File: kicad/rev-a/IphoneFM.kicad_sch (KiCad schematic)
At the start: 102 parts, among them J1 USB 2.0 Type-C, J2 SMA jack, SW1 SPDT, SW2 SPST, SW3 6 × SPST, U1 MCU, U2 Synthesizer, U3 3.3 V 600 mA LDO, U4 FM receiver, U5 SPDT RF switch, U6 USB ESD array, U7 Digital step attenuator, Y2 20 MHz CMOS XO

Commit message: Step 2.6: IphoneFM footprints assigned to all 102 symbols
Co-Authored-By: Claude Opus 5.5 <noreply@anthropic.com>
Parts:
- C1, C2, C23, C27, C8: footprint Capacitor_SMD:C_0603_1608Metric -> IphoneFM:C_0603_1608Metric
- C10, C11, C13, C14, C15, C16, C17, C18, C19, C20, C21, C22, C24, C25, C26, C28, C29, C30, C31, C32, C33, C34, C35, C36, C37, C38, C39, C4, C40, C41, C5, C6, C7: footprint Capacitor_SMD:C_0402_1005Metric -> IphoneFM:C_0402_1005Metric
- C12, C3, C9: footprint Capacitor_SMD:C_0805_2012Metric -> IphoneFM:C_0805_2012Metric
- D1: footprint (none) -> IphoneFM:LED_RGB_XINGLIGHT_XL-1615RGBC_1.6x1.5mm
- D3, D4: footprint Package_SON:Texas_DPY0002A_0.6x1mm_P0.65mm -> IphoneFM:Texas_DPY0002A_0.6x1mm_P0.65mm
- D5: footprint (none) -> IphoneFM:D_SOD-882
- FB1, FB2, FB3: footprint Inductor_SMD:L_0402_1005Metric -> IphoneFM:L_0402_1005Metric
- J1: footprint (none) -> IphoneFM:USB_C_Receptacle_HRO_TYPE-C-31-M-12_2020
- J2: footprint (none) -> IphoneFM:SMA_BAT_Wireless_BWSMA-KWE-Z001
- L1, L2, L3: footprint Inductor_SMD:L_0603_1608Metric -> IphoneFM:L_0603_1608Metric
- R1, R10, R11, R12, R13, R14, R15, R16, R17, R18, R19, R2, R20, R21, R22, R23, R24, R25, R26, R27, R3, R4, R5, R6, R7, R8, R9: footprint Resistor_SMD:R_0402_1005Metric -> IphoneFM:R_0402_1005Metric
- RV1, RV2, RV3: footprint (none) -> IphoneFM:Potentiometer_Alps_RK10J_Reflow_Thumbwheel_14mm
- SW1: footprint (none) -> IphoneFM:SW_SPDT_Shouhan_MSK12C02_Tabs4
- SW2: footprint (none) -> IphoneFM:SW_SPST_EVQP7A
- SW3: footprint (none) -> IphoneFM:SW_DIP_SPSTx06_Side_CK_TDP06H1SBD1_W7.62mm_P1.27mm
- TP1, TP2, TP3, TP4, TP5, TP6, TP7, TP8: footprint TestPoint:TestPoint_Pad_D1.5mm -> IphoneFM:TestPoint_Pad_D1.5mm
- U1: footprint Package_DFN_QFN:QFN-48-1EP_7x7mm_P0.5mm_EP5.6x5.6mm -> IphoneFM:QFN-48-1EP_7x7mm_P0.5mm_EP5.6x5.6mm
- U2: footprint (none) -> IphoneFM:TI_NJK0036A_WQFN-36-1EP_6x6mm_P0.5mm_EP4.6x4.6mm
- U3: footprint Package_TO_SOT_SMD:SOT-23-5 -> IphoneFM:SOT-23-5
- U4: footprint (none) -> IphoneFM:SiliconLabs_QFN-20-1EP_3x3mm_P0.5mm_EP1.8x1.8mm
- U5: footprint (none) -> IphoneFM:SOT-363_SC-70-6
- U6: footprint Package_TO_SOT_SMD:SOT-23-6 -> IphoneFM:SOT-23-6
- U7: footprint (none) -> IphoneFM:QFN-24-1EP_4x4mm_P0.5mm_EP2.75x2.75mm
- Y2: footprint (none) -> IphoneFM:Oscillator_SMD_SiT_PQFN-4Pin_3.2x2.5mm

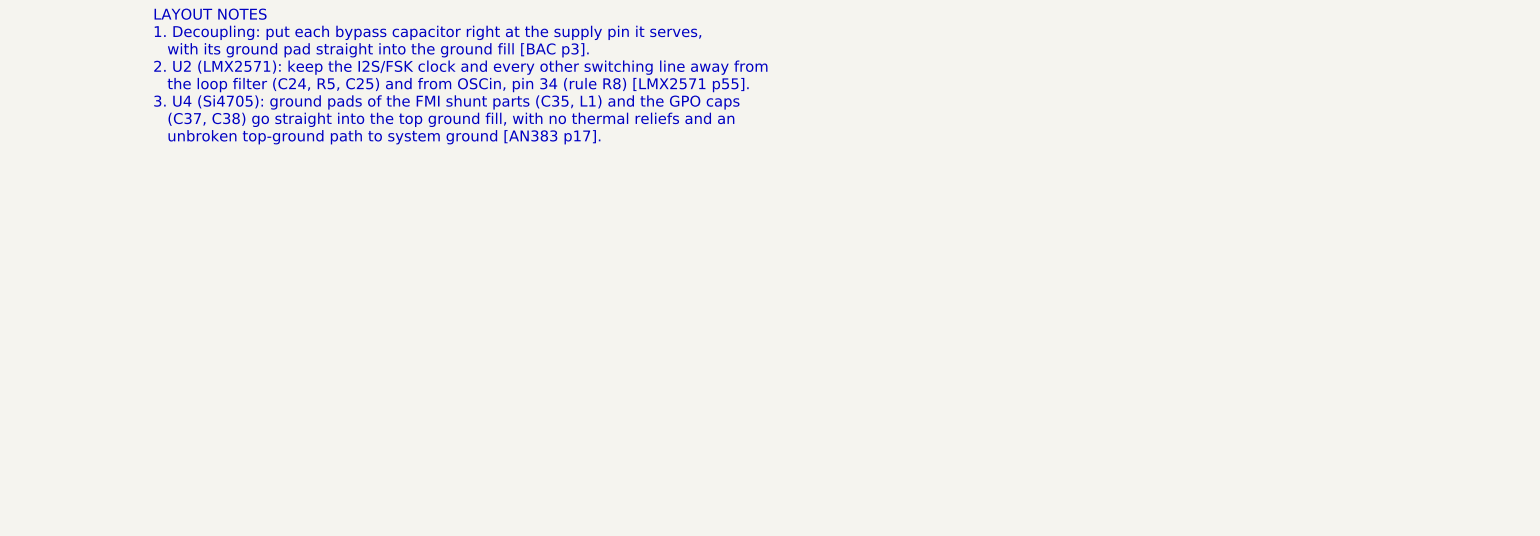
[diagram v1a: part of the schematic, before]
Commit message: Step 3.5: mounting holes H1-H4 in netlist.json, on the schematic, with an M2 footprint
Co-Authored-By: Claude Opus 5.5 <noreply@anthropic.com>
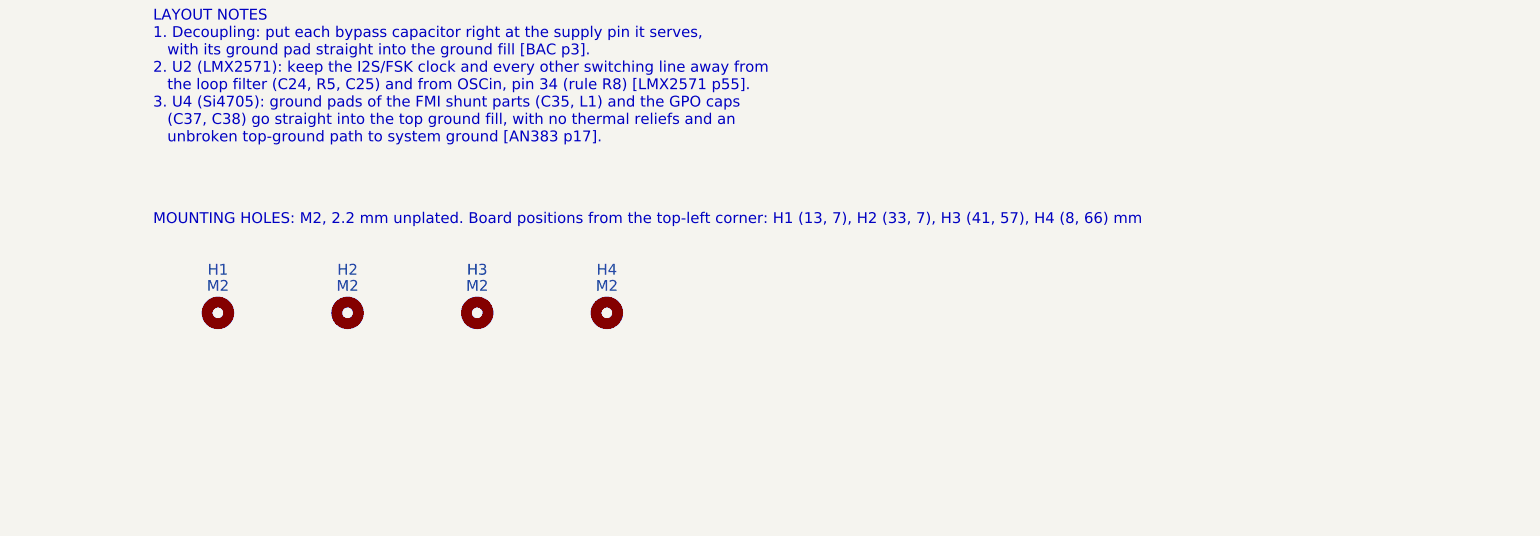
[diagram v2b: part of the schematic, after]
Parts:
- added H1, H2, H3, H4: M2, IphoneFM:MountingHole_2.2mm_M2, symbol Mechanical:MountingHole
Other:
- note added: "MOUNTING HOLES: M2, 2.2 mm unplated. Board positions from the top-left corner: H1 (13, 7), H2 (33, 7), H3 (41, 57), H4 (8, 66) mm"
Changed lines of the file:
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@@
 		(effects (font (size 1.27 1.27)) (justify left top))
+	)
+	(symbol
+		(lib_id "Mechanical:MountingHole")
+		(at 452.12 358.14 0)
+		(unit 1)
+		(exclude_from_sim no)
+		(in_bom no)
+		(on_board yes)
+		(dnp no)
+		(property "Reference" "H1"
+			(at 452.12 353.06 0)
+			(effects (font (size 1.27 1.27)))
+		)
+		(property "Value" "M2"
+			(at 452.12 354.96 0)
+			(effects (font (size 1.27 1.27)))
+		)
+		(property "Footprint" "IphoneFM:MountingHole_2.2mm_M2"
+			(at 452.12 358.14 0)
+			(effects (font (size 1.27 1.27)) (hide yes))
+		)
+		(property "Datasheet" "~"
+			(at 452.12 358.14 0)
+			(effects (font (size 1.27 1.27)) (hide yes))
+		)
+		(instances
+			(project "IphoneFM"
+				(path "/efee88c9-028d-4fdb-86e0-0a4145b330e1"
+					(reference "H1") (unit 1)
+				)
+			)
+		)
+	)
+	(symbol
+		(lib_id "Mechanical:MountingHole")
+		(at 467.36 358.14 0)
+		(unit 1)
+		(exclude_from_sim no)
+		(in_bom no)
+		(on_board yes)
+		(dnp no)
+		(property "Reference" "H2"
+			(at 467.36 353.06 0)
+			(effects (font (size 1.27 1.27)))
+		)
+		(property "Value" "M2"
+			(at 467.36 354.96 0)
+			(effects (font (size 1.27 1.27)))
+		)
+		(property "Footprint" "IphoneFM:MountingHole_2.2mm_M2"
+			(at 467.36 358.14 0)
+			(effects (font (size 1.27 1.27)) (hide yes))
+		)
+		(property "Datasheet" "~"
+			(at 467.36 358.14 0)
+			(effects (font (size 1.27 1.27)) (hide yes))
+		)
+		(instances
+			(project "IphoneFM"
+				(path "/efee88c9-028d-4fdb-86e0-0a4145b330e1"
+					(reference "H2") (unit 1)
+				)
+			)
+		)
+	)
+	(symbol
+		(lib_id "Mechanical:MountingHole")
+		(at 482.60 358.14 0)
+		(unit 1)
+		(exclude_from_sim no)
+		(in_bom no)
+		(on_board yes)
+		(dnp no)
+		(property "Reference" "H3"
+			(at 482.60 353.06 0)
+			(effects (font (size 1.27 1.27)))
+		)
+		(property "Value" "M2"
+			(at 482.60 354.96 0)
+			(effects (font (size 1.27 1.27)))
+		)
+		(property "Footprint" "IphoneFM:MountingHole_2.2mm_M2"
+			(at 482.60 358.14 0)
+			(effects (font (size 1.27 1.27)) (hide yes))
+		)
+		(property "Datasheet" "~"
+			(at 482.60 358.14 0)
+			(effects (font (size 1.27 1.27)) (hide yes))
+		)
+		(instances
+			(project "IphoneFM"
+				(path "/efee88c9-028d-4fdb-86e0-0a4145b330e1"
+					(reference "H3") (unit 1)
+				)
+			)
+		)
+	)
+	(symbol
+		(lib_id "Mechanical:MountingHole")
+		(at 497.84 358.14 0)
+		(unit 1)
+		(exclude_from_sim no)
+		(in_bom no)
+		(on_board yes)
+		(dnp no)
+		(property "Reference" "H4"
+			(at 497.84 353.06 0)
+			(effects (font (size 1.27 1.27)))
+		)
+		(property "Value" "M2"
+			(at 497.84 354.96 0)
+			(effects (font (size 1.27 1.27)))
+		)
+		(property "Footprint" "IphoneFM:MountingHole_2.2mm_M2"
+			(at 497.84 358.14 0)
+			(effects (font (size 1.27 1.27)) (hide yes))
+		)
+		(property "Datasheet" "~"
+			(at 497.84 358.14 0)
+			(effects (font (size 1.27 1.27)) (hide yes))
+		)
+		(instances
+			(project "IphoneFM"
+				(path "/efee88c9-028d-4fdb-86e0-0a4145b330e1"
+					(reference "H4") (unit 1)
+				)
+			)
+		)
+	)
+	(text "MOUNTING HOLES: M2, 2.2 mm unplated. Board positions from the top-left corner: H1 (13, 7), H2 (33, 7), H3 (41, 57), H4 (8, 66) mm"
+		(exclude_from_sim no)
+		(at 444.50 347.98 0)
+		(effects (font (size 1.27 1.27)) (justify left bottom))
 	)
 	(sheet_instances

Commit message: Phase 5: U1 MICROWIRE pins reordered (28 MUX, 27 CLK, 26 DATA, 25 LE, driven by GPIO) so the four lines reach U2 with no crossing; C5 and R6-R8 moved for routing room; parts provenance list; R6-R8 placement trial and board view tools
Co-Authored-By: Claude Opus 5.5 <noreply@anthropic.com>
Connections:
- net LMX_CLK: now also U1.27 (PB14); no longer U1.26 (PB13)
- net LMX_DATA: now also U1.26 (PB13); no longer U1.28 (PB15)
- net LMX_MUX: now also U1.28 (PB15); no longer U1.27 (PB14)
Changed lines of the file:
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@@
 		(stroke (width 0) (type default))
 	)
-	(label "LMX_CLK"
+	(label "LMX_DATA"
 		(at 205.74 274.32 180)
 		(effects (font (size 1.27 1.27)) (justify right bottom))
@@
 		(stroke (width 0) (type default))
 	)
-	(label "LMX_DATA"
+	(label "LMX_MUX"
 		(at 205.74 279.40 180)
 		(effects (font (size 1.27 1.27)) (justify right bottom))
@@
 		(stroke (width 0) (type default))
 	)
-	(label "LMX_MUX"
+	(label "LMX_CLK"
 		(at 205.74 276.86 180)
 		(effects (font (size 1.27 1.27)) (justify right bottom))

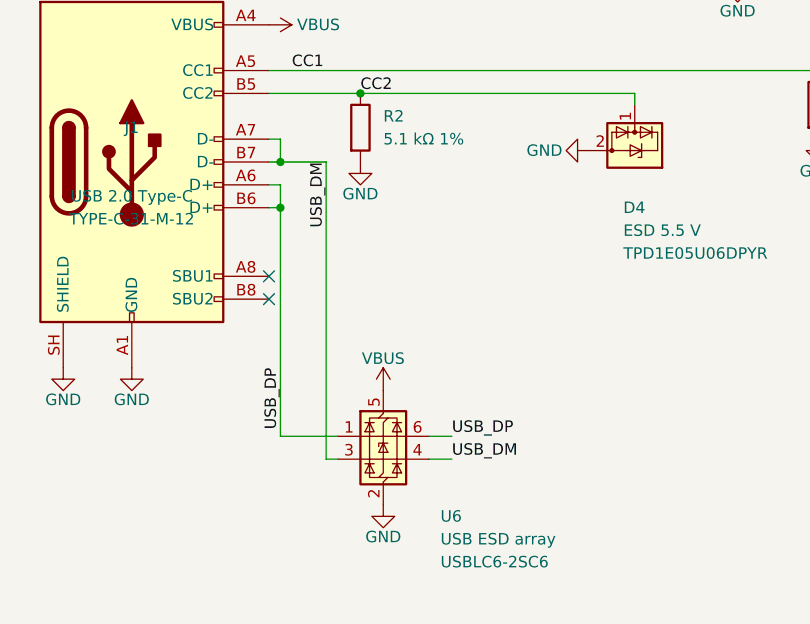
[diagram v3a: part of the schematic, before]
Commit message: Phase 5: U1 right side routed: seven-line bus to U2 (MICROWIRE straight in, FSK through R6-R8 to U2's entry vias), USB and SWD crossing under it on short bottom-layer hops; U6 channels and TP7/TP8 places swapped so nothing crosses; ATT_IN bend moved toward C26; router fix (vias were placed at grid indices) and bottom-layer cost; DRC tool
Co-Authored-By: Claude Opus 5.5 <noreply@anthropic.com>
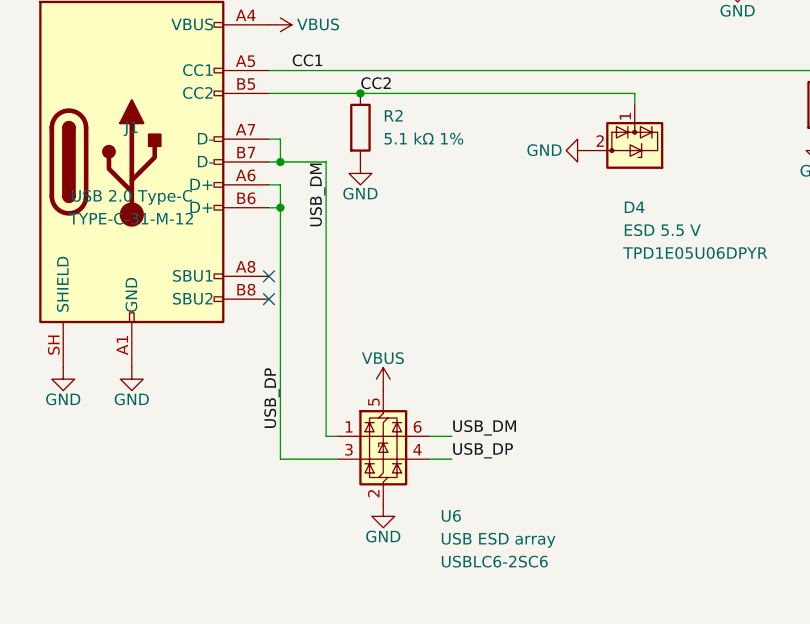
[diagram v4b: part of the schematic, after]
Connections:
- net USB_DM: now also U6.1 (I/O1), U6.6 (I/O1); no longer U6.3 (I/O2), U6.4 (I/O2)
- net USB_DP: now also U6.3 (I/O2), U6.4 (I/O2); no longer U6.1 (I/O1), U6.6 (I/O1)
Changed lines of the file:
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@@
 	)
 	(wire
-		(pts (xy 54.61 76.20) (xy 54.61 101.60))
+		(pts (xy 54.61 76.20) (xy 54.61 104.14))
 		(stroke (width 0) (type default))
 	)
@@
 	)
 	(wire
-		(pts (xy 60.96 101.60) (xy 54.61 101.60))
+		(pts (xy 60.96 104.14) (xy 54.61 104.14))
 		(stroke (width 0) (type default))
 	)
@@
 	)
 	(wire
-		(pts (xy 59.69 71.12) (xy 59.69 104.14))
+		(pts (xy 59.69 71.12) (xy 59.69 101.60))
 		(stroke (width 0) (type default))
 	)
@@
 	)
 	(wire
-		(pts (xy 60.96 104.14) (xy 59.69 104.14))
+		(pts (xy 60.96 101.60) (xy 59.69 101.60))
 		(stroke (width 0) (type default))
 	)
@@
 		(stroke (width 0) (type default))
 	)
-	(label "USB_DM"
+	(label "USB_DP"
 		(at 73.66 104.14 0)
 		(effects (font (size 1.27 1.27)) (justify left bottom))
@@
 		(stroke (width 0) (type default))
 	)
-	(label "USB_DP"
+	(label "USB_DM"
 		(at 73.66 101.60 0)
 		(effects (font (size 1.27 1.27)) (justify left bottom))
